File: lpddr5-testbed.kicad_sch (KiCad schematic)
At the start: 2 parts

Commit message: Loclib
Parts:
- R1, R2: footprint antmicro-footprints:R_0402_1005Metric -> lpddr5-testbed-footprints:R_0402_1005Metric; symbol antmicroResistors0402:R_100R_0402 -> lpddr5-testbed:R_100R_0402

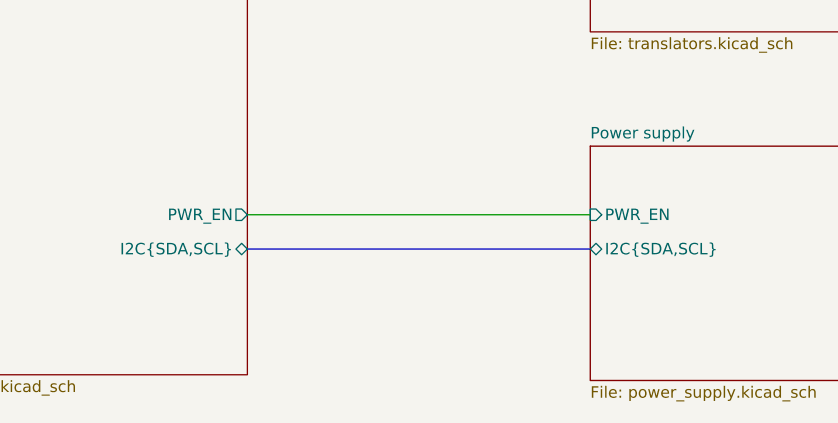
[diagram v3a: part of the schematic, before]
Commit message: [#53267] schematic: improve power supply sequencing and power good signal
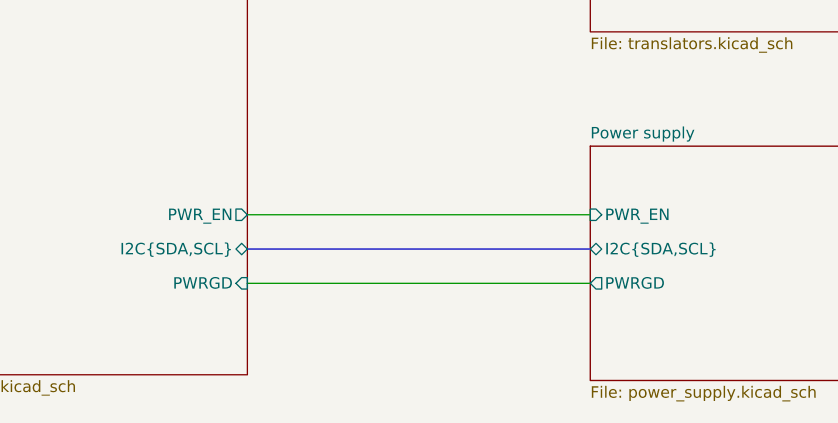
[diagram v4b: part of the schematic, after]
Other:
- sheet Power supply ports: added PWRGD; removed none
- sheet SODIMM ports: added PWRGD; removed none
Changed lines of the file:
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@@
+    (stroke (width 0) (type default) (color 0 0 0 0))
+  )
+  (wire (pts (xy 146.05 193.04) (xy 184.15 193.04))
     (stroke (width 0) (type default) (color 0 0 0 0))
   )
@@
       (effects (font (size 1.27 1.27)) (justify right))
     )
+    (pin "PWRGD" input (at 146.05 193.04 0)
+      (effects (font (size 1.27 1.27)) (justify right))
+    )
   )
   (sheet (at 247.65 101.6) (size 41.91 25.4) (fields_autoplaced)
@@
     )
     (pin "PWR_EN" input (at 184.15 185.42 180)
+      (effects (font (size 1.27 1.27)) (justify left))
+    )
+    (pin "PWRGD" output (at 184.15 193.04 180)
       (effects (font (size 1.27 1.27)) (justify left))
     )
@@
       (reference "#PWR0101") (unit 1) (value "GND") (footprint "")
     )
+    (path "/6dc6d680-4b07-4d6c-9fb2-b5a24aa4dc23/56c872e4-9c8c-4a1b-9094-c4706673ff8d"
+      (reference "#PWR0102") (unit 1) (value "+1V1") (footprint "")
+    )
     (path "/afd026d6-1a56-4fdd-8c33-af6dc6bd4334/75a98f04-2722-4937-a614-62aefca1a576"
       (reference "#PWR0103") (unit 1) (value "GND") (footprint "")
@@
       (reference "#PWR0225") (unit 1) (value "GND") (footprint "")
     )
-    (path "/6dc6d680-4b07-4d6c-9fb2-b5a24aa4dc23/6b5800dc-5154-4d34-8ec1-37538a24a585"
-      (reference "#PWR0270") (unit 1) (value "+1V8") (footprint "")
-    )
     (path "/00000000-0000-0000-0000-00005ff943ac/96ce219f-5696-4871-8db2-1eed6bfc649d"
       (reference "#PWR0271") (unit 1) (value "GND") (footprint "")
@@
       (reference "R2") (unit 1) (value "R_100R_0402") (footprint "lpddr5-testbed-footprints:R_0402_1005Metric")
     )
+    (path "/6dc6d680-4b07-4d6c-9fb2-b5a24aa4dc23/607ffe01-e8f2-4613-aa20-a0ab14ebad31"
+      (reference "R3") (unit 1) (value "R_0R_0402") (footprint "lpddr5-testbed-footprints:R_0402_1005Metric")
+    )
     (path "/afd026d6-1a56-4fdd-8c33-af6dc6bd4334/da106cb8-97e7-4a19-8bd9-4d16246e9819"
       (reference "R4") (unit 1) (value "R_4x100R_0402_array") (footprint "lpddr5-testbed-footprints:R_Array_4x0402_Panasonic_EXB28V")
@@
       (reference "R29") (unit 1) (value "R_0R_0402") (footprint "lpddr5-testbed-footprints:R_0402_1005Metric")
     )
-    (path "/6dc6d680-4b07-4d6c-9fb2-b5a24aa4dc23/32f9b6c4-c055-4253-8176-2288143dab41"
-      (reference "R30") (unit 1) (value "R_100k_0402") (footprint "lpddr5-testbed-footprints:R_0402_1005Metric")
-    )
     (path "/6dc6d680-4b07-4d6c-9fb2-b5a24aa4dc23/2d9cbb29-f69f-4727-be13-15cbda03aaf9"
       (reference "R31") (unit 1) (value "R_25k5_0402") (footprint "lpddr5-testbed-footprints:R_0402_1005Metric")
@@
       (reference "TP3") (unit 1) (value "TP_1mm_SMD") (footprint "lpddr5-testbed-footprints:TP_SMD_1mm")
     )
+    (path "/6dc6d680-4b07-4d6c-9fb2-b5a24aa4dc23/cb8bd187-6902-4577-8c05-1473acf607e4"
+      (reference "TP4") (unit 1) (value "TP_0.75mm_SMD") (footprint "lpddr5-testbed-footprints:TP_SMD_0.75mm")
+    )
+    (path "/6dc6d680-4b07-4d6c-9fb2-b5a24aa4dc23/0c677b03-d461-49f7-8de3-8f27412d1537"
+      (reference "TP5") (unit 1) (value "TP_0.75mm_SMD") (footprint "lpddr5-testbed-footprints:TP_SMD_0.75mm")
+    )
+    (path "/6dc6d680-4b07-4d6c-9fb2-b5a24aa4dc23/e8572542-2ddf-4aee-8040-65ce6266bc8e"
+      (reference "TP6") (unit 1) (value "TP_0.75mm_SMD") (footprint "lpddr5-testbed-footprints:TP_SMD_0.75mm")
+    )
+    (path "/6dc6d680-4b07-4d6c-9fb2-b5a24aa4dc23/f555dd8c-f694-45a3-8af1-7d53aad85957"
+      (reference "TP7") (unit 1) (value "TP_0.75mm_SMD") (footprint "lpddr5-testbed-footprints:TP_SMD_0.75mm")
+    )
+    (path "/6dc6d680-4b07-4d6c-9fb2-b5a24aa4dc23/67492140-899c-4010-94b1-1e80fd9a9721"
+      (reference "TP8") (unit 1) (value "TP_0.75mm_SMD") (footprint "lpddr5-testbed-footprints:TP_SMD_0.75mm")
+    )
     (path "/00000000-0000-0000-0000-00005ff943ac/a542b0b1-3526-4197-89e0-7544f3a8300c"

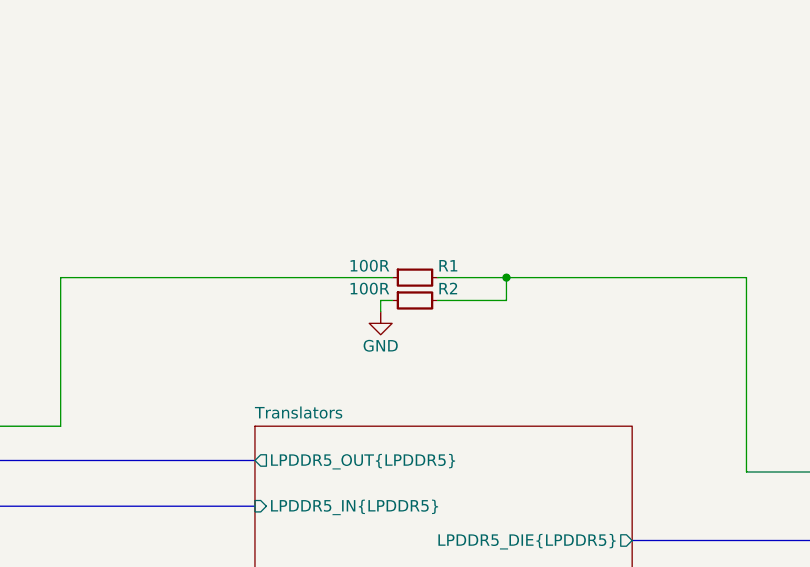
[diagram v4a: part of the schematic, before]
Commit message: [#53670] sch: remove not needed voltage divider
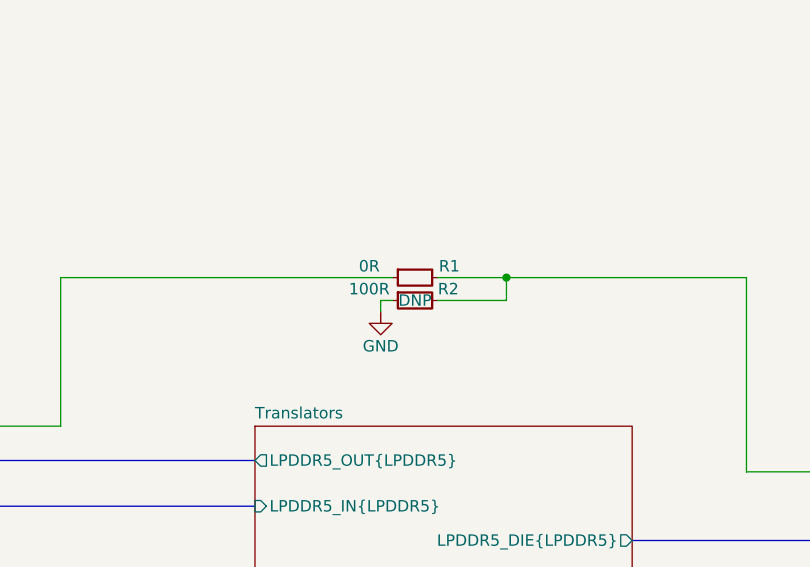
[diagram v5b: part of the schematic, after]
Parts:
- removed R1: R_100R_0402, lpddr5-testbed-footprints:R_0402_1005Metric, symbol lpddr5-testbed:R_100R_0402
- added R1: R_0R_0402, antmicro-footprints:R_0402_1005Metric, symbol antmicroResistors0402:R_0R_0402
- R2: DNP (none) -> DNP
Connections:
- net LPDDR5/~{RESET}: now also R1.2
- net SODIMM/~{RESET}: now also R1.1
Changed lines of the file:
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@@
     (effects (font (size 2.4892 2.4892) (thickness 0.4978) bold) (justify left bottom))
+  )
+  (symbol (lib_id "antmicroResistors0402:R_0R_0402") (at 199.39 85.09 0) (unit 1)
+    (in_bom yes) (on_board yes)
+    (property "Reference" "R1" (id 0) (at 205.74 83.82 0)
+      (effects (font (size 1.27 1.27) (thickness 0.15)))
+    )
+    (property "Value" "R_0R_0402" (id 1) (at 219.71 97.79 0)
+      (effects (font (size 1.27 1.27) (thickness 0.15)) (justify left bottom) hide)
+    )
+    (property "Footprint" "antmicro-footprints:R_0402_1005Metric" (id 2) (at 219.71 100.33 0)
+      (effects (font (size 1.27 1.27) (thickness 0.15)) (justify left bottom) hide)
+    )
+    (property "Datasheet" "https://industrial.panasonic.com/cdbs/www-data/pdf/RDA0000/AOA0000C301.pdf" (id 3) (at 219.71 102.87 0)
+      (effects (font (size 1.27 1.27) (thickness 0.15)) (justify left bottom) hide)
+    )
+    (property "MPN" "ERJ2GE0R00X" (id 4) (at 219.71 105.41 0)
+      (effects (font (size 1.27 1.27) (thickness 0.15)) (justify left bottom) hide)
+    )
+    (property "Manufacturer" "Panasonic" (id 5) (at 219.71 107.95 0)
+      (effects (font (size 1.27 1.27) (thickness 0.15)) (justify left bottom) hide)
+    )
+    (property "License" "Apache-2.0" (id 6) (at 219.71 110.49 0)
+      (effects (font (size 1.27 1.27) (thickness 0.15)) (justify left bottom) hide)
+    )
+    (property "Author" "Antmicro" (id 7) (at 219.71 113.03 0)
+      (effects (font (size 1.27 1.27) (thickness 0.15)) (justify left bottom) hide)
+    )
+    (property "Val" "0R" (id 8) (at 196.85 83.82 0)
+      (effects (font (size 1.27 1.27) (thickness 0.15)))
+    )
+    (property "Tolerance" "~" (id 9) (at 219.71 95.25 0)
+      (effects (font (size 1.27 1.27)) (justify left bottom) hide)
+    )
+    (property "Current" "1A" (id 10) (at 219.71 115.57 0)
+      (effects (font (size 1.27 1.27) (thickness 0.15)) (justify left bottom) hide)
+    )
+    (pin "1")
+    (pin "2")
   )
   (symbol (lib_id "lpddr5-testbed:R_100R_0402") (at 199.39 87.63 0) (unit 1)
@@
       (effects (font (size 1.27 1.27)) (justify left bottom) hide)
     )
+    (property "DNP" "DNP" (id 10) (at 201.93 87.63 0))
     (pin "1")
     (pin "2")
@@
     )
     (pin "1")
-  )
-  (symbol (lib_id "lpddr5-testbed:R_100R_0402") (at 199.39 85.09 0) (unit 1)
-    (in_bom yes) (on_board yes)
-    (property "Reference" "R1" (id 0) (at 204.47 83.82 0)
-      (effects (font (size 1.27 1.27) (thickness 0.15)) (justify left))
-    )
-    (property "Value" "R_100R_0402" (id 1) (at 219.71 97.79 0)
-      (effects (font (size 1.27 1.27) (thickness 0.15)) (justify left bottom) hide)
-    )
-    (property "Footprint" "lpddr5-testbed-footprints:R_0402_1005Metric" (id 2) (at 219.71 100.33 0)
-      (effects (font (size 1.27 1.27) (thickness 0.15)) (justify left bottom) hide)
-    )
-    (property "Datasheet" "https://www.bourns.com/docs/product-datasheets/cr.pdf" (id 3) (at 219.71 102.87 0)
-      (effects (font (size 1.27 1.27) (thickness 0.15)) (justify left bottom) hide)
-    )
-    (property "MPN" "CR0402-FX-1000GLF" (id 4) (at 219.71 105.41 0)
-      (effects (font (size 1.27 1.27) (thickness 0.15)) (justify left bottom) hide)
-    )
-    (property "Manufacturer" "Bourns" (id 5) (at 219.71 107.95 0)
-      (effects (font (size 1.27 1.27) (thickness 0.15)) (justify left bottom) hide)
-    )
-    (property "License" "Apache-2.0" (id 6) (at 219.71 110.49 0)
-      (effects (font (size 1.27 1.27) (thickness 0.15)) (justify left bottom) hide)
-    )
-    (property "Author" "Antmicro" (id 7) (at 219.71 113.03 0)
-      (effects (font (size 1.27 1.27) (thickness 0.15)) (justify left bottom) hide)
-    )
-    (property "Val" "100R" (id 8) (at 196.85 83.82 0)
-      (effects (font (size 1.27 1.27) (thickness 0.15)))
-    )
-    (property "Tolerance" "1%" (id 9) (at 219.71 95.25 0)
-      (effects (font (size 1.27 1.27)) (justify left bottom) hide)
-    )
-    (pin "1")
-    (pin "2")
   )
   (sheet (at 108.585 95.25) (size 37.465 107.95) (fields_autoplaced)
@@
       (reference "Q2") (unit 1) (value "DMG1012T-7") (footprint "lpddr5-testbed-footprints:SOT-523")
     )
-    (path "/db5eb0da-5782-4ec3-a730-40f46b7b0585"
-      (reference "R1") (unit 1) (value "R_100R_0402") (footprint "lpddr5-testbed-footprints:R_0402_1005Metric")
+    (path "/314edb86-b83c-439b-a492-7e76c4d24d52"
+      (reference "R1") (unit 1) (value "R_0R_0402") (footprint "antmicro-footprints:R_0402_1005Metric")
     )
     (path "/36feb2bc-19fd-4c1a-bb5d-109d9c08ceb3"
